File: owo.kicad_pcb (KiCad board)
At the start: 2 copper layers, 10.4 x 8.1 mm, 145 parts, among them J1 SJ-43515RS-SMT-TR, J2 SJ-43515RS-SMT-TR, J3 5051102291, J4 503398-1892, J5 2171840001, Q1 PMOS, Q2 NMOS, SW1 KMR221GLFS, SW2 KMR221GLFS, SW3 KMR221GLFS, SW4 KMR221GLFS, SW5 KMR221GLFS, SW6 KMR221GLFS, SW7 KMR221GLFS, U1 BQ24074RGT, U10 MCP23017_ML, U11 ESP32-C6-WROOM-1, U12 KMR241GLFS, U13 KMR241GLFS, U14 OPA1622, U2 TPS7A20xxxDQN, U3 LM27762, U4 TPS62840DLCR, U5 CD74HC4067M, U6 PCM5122PW, U7 OPA1622, U8 KMR241GLFS, U9 KMR241GLFS, X1 ASE-45.1584MHz, X2 ASE-24.576MHz, Y1 32.768kHz 9pF

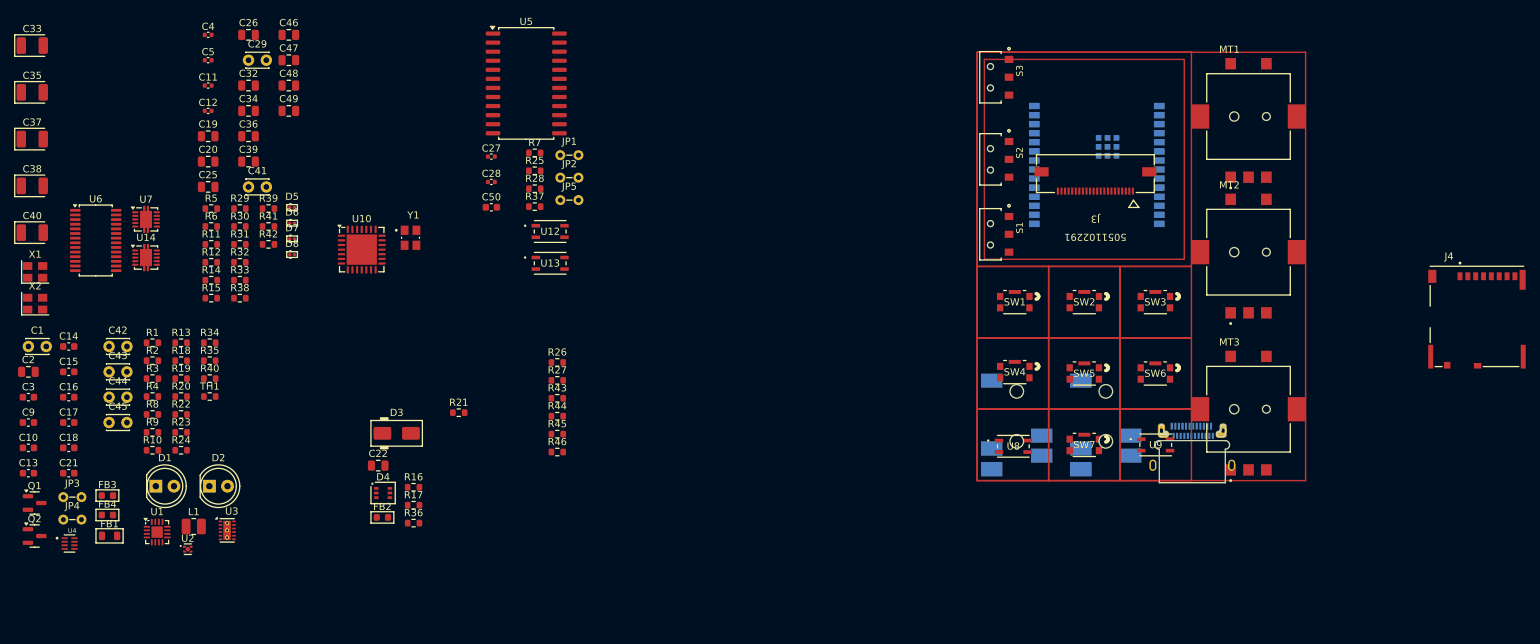
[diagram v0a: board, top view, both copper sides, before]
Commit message: ICs placed
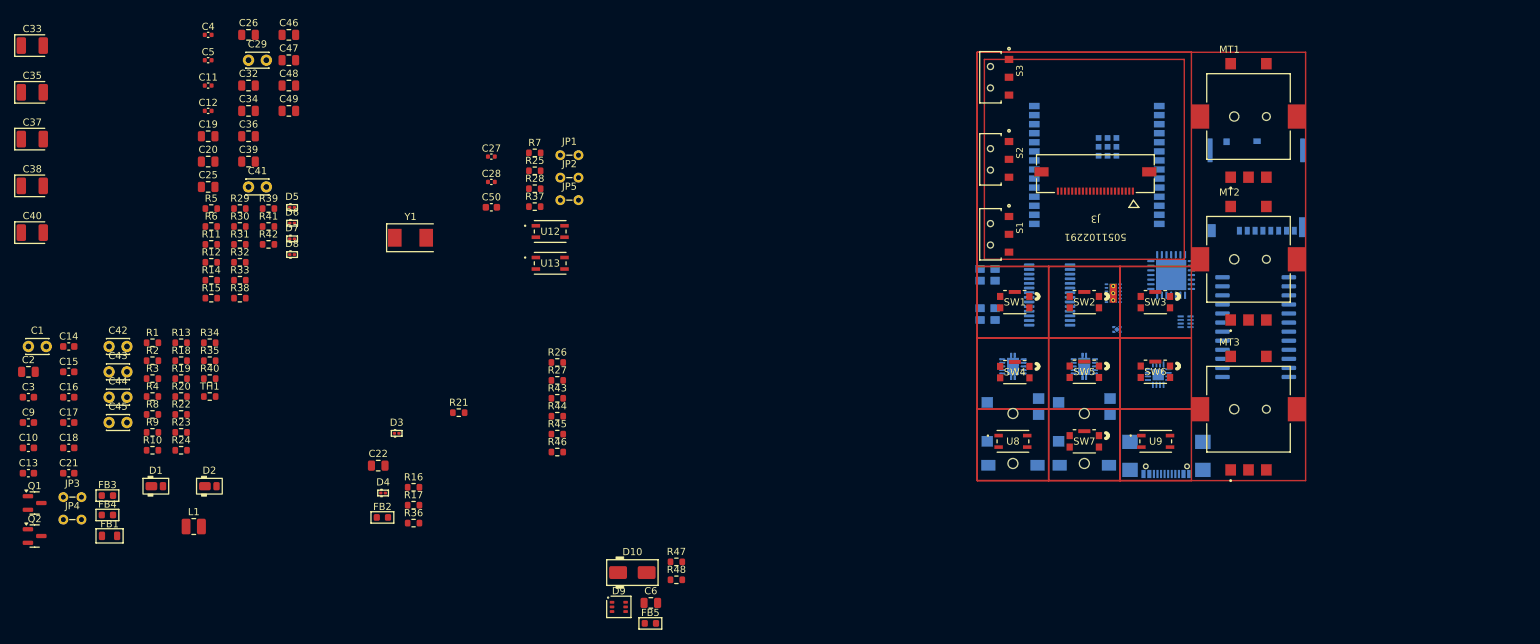
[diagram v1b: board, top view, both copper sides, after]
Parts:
- removed J5: 2171840001, uwu:MOLEX_2171840001
- added C6: 10uF/25V, Capacitor_SMD:C_0805_2012Metric, F.Cu at (100.3, 112.1)
- added D10: SS14, PCM_Diode_SMD_AKL:D_SMA, F.Cu at (97.7, 107.9)
- added D9: SMF05CT, PCM_Package_TO_SOT_SMD_AKL:SOT-363_SC-70-6, F.Cu at (95.8, 112.7)
- added FB5: 220@100MHz, PCM_Ferrite_SMD_AKL:Ferrite_0603_1608Metric, F.Cu at (100.2, 115.0)
- added J6: USB4110GFA, uwu:GCT_USB4110GFA, B.Cu at (172.5, 93.0)
- added R47: 1.1k, Resistor_SMD:R_0603_1608Metric, F.Cu at (103.9, 106.4)
- added R48: 1.1k, Resistor_SMD:R_0603_1608Metric, F.Cu at (103.9, 108.9)
- D1, D2: footprint LED_THT:LED_D5.0mm -> PCM_LED_SMD_AKL:LED_PLCC-2_2216
- D3: value SS14 -> SP1005-01WTG; footprint PCM_Diode_SMD_AKL:D_SMA -> PCM_Diode_SMD_AKL:D_0201_0603Metric
- D4: value SMF05CT -> SP1005-01WTG; footprint PCM_Package_TO_SOT_SMD_AKL:SOT-363_SC-70-6 -> PCM_Diode_SMD_AKL:D_0201_0603Metric
- J1, J2: value SJ-43515RS-SMT-TR -> SJ-43516-SMT-TR; footprint uwu:CUI_SJ-43515RS-SMT-TR -> uwu:CUI_SJ2-35894D-SMT-TR
- J4, U1, U10, U14, U2, U3, U4, U5, U6, U7, X1, X2: moved to B.Cu
- R14, R15: value 100 -> 10
- Y1: footprint uwu:XTAL_ASE-24.576MHZ-LC-T -> Crystal:Crystal_SMD_0603-2Pin_6.0x3.5mm
- moved U4 159.4 mm to (175.2, 72.8), turned to 180 degrees
- moved U1 142.0 mm to (171.4, 80.2), turned to 180 degrees
- moved U6 133.8 mm to (156.1, 69.0), turned to 180 degrees
- moved U2 133.7 mm to (165.6, 73.8), turned to 180 degrees
- moved X2 133.4 mm to (147.4, 71.7), turned to 180 degrees
- moved X1 133.4 mm to (147.4, 66.2), turned to 180 degrees
- moved U7 133.0 mm to (161.0, 79.0), turned to 180 degrees
- moved U3 128.5 mm to (165.1, 68.8), turned to 180 degrees
- moved U14 122.4 mm to (151.0, 79.0), turned to 180 degrees
- moved U10 113.4 mm to (173.2, 66.2), turned to 180 degrees
- moved U5 107.7 mm to (185.0, 73.5), turned to 180 degrees
- moved J4 35.6 mm to (185.1, 54.4)
- moved J2 13.7 mm to (161.0, 89.0)
- moved J1 10.5 mm to (151.0, 89.0)
- moved MT2 1.00 mm to (184.0, 64.0)
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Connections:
- D3 pad 2: USB_VBUS -> AGND
- D4 pad 1: USB_VBUS -> Net-(D4-K)
- D4 pad 2: GND -> AGND
- J1 pad 2: Net-(D8-K) -> Net-(D4-K)
- J1 pad 3: Net-(D7-K) -> Net-(D3-K)
- R14 pad 2: Net-(D8-K) -> Net-(D4-K)
- R15 pad 1: LINEOUT_L -> LINEOUT_R
- R15 pad 2: Net-(D7-K) -> Net-(D3-K)
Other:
- board outline removed

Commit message: all pcb elements positioned + minor schematics changes
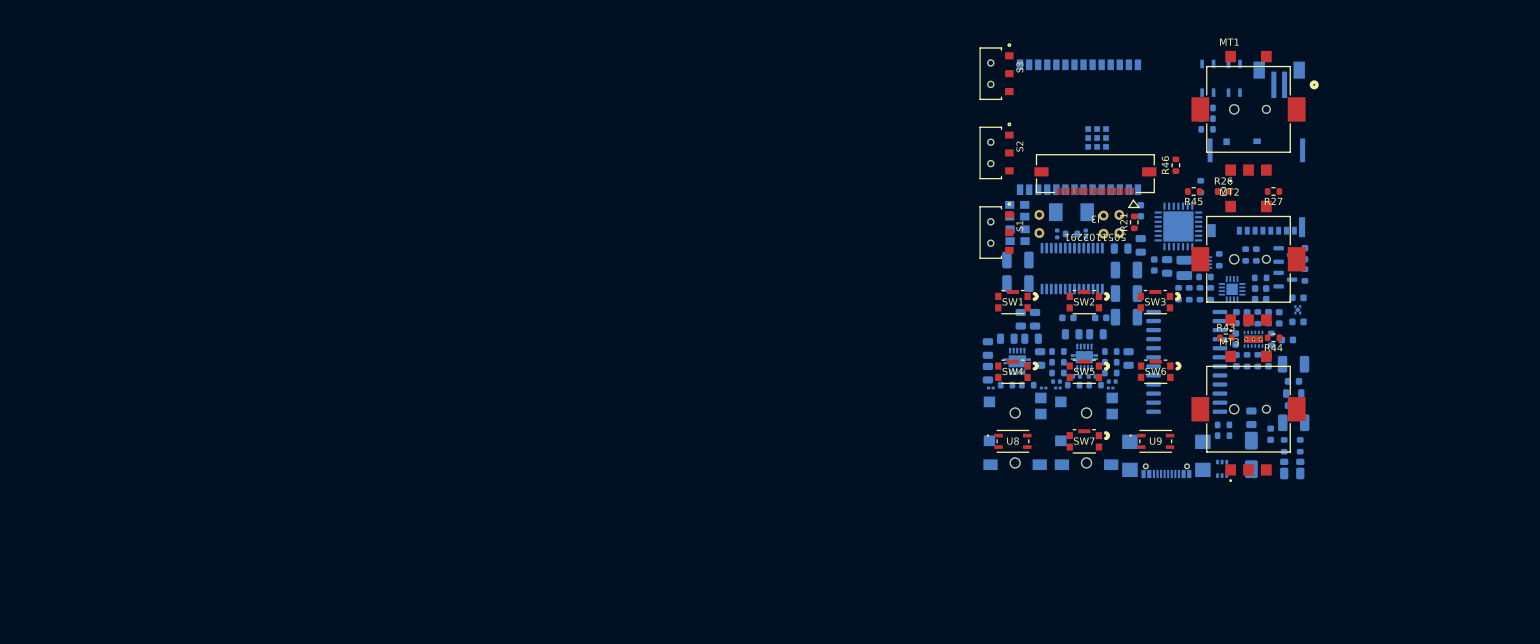
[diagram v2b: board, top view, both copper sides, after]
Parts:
- removed C22: 10uF/25V, Capacitor_SMD:C_0805_2012Metric
- removed D7, D8: SP1005-01WTG, PCM_Diode_SMD_AKL:D_0201_0603Metric
- removed FB2: 220@100MHz, PCM_Ferrite_SMD_AKL:Ferrite_0603_1608Metric
- removed JP3, JP4: Jumper_2_Bridged, PCM_Jumper_AKL:Jumper_P2.54mm_D0.7mm
- removed R16, R17: 1.1k, Resistor_SMD:R_0603_1608Metric
- removed R20: 10k, Resistor_SMD:R_0603_1608Metric
- removed R33, R38, R39, R41, R42: 0, Resistor_SMD:R_0603_1608Metric
- added J5: 3.7V, uwu:CONN_B2B-ZR-SM4-TF_JST, B.Cu at (189.0, 39.6)
- C1: value Capacitor_NP -> 1uF; footprint Capacitor_THT:C_Disc_D3.0mm_W2.0mm_P2.50mm -> Capacitor_SMD:C_0603_1608Metric; moved to B.Cu
- C10, C11, C12, C13, C14, C15, C16, C17, C18, C19, C2, C20, C21, C25, C26, C27, C28, C3, C32, C33, C34, C35, C36, C37, C38, C39, C4, C40, C46, C47, C48, C49, C5, C50, C6, C9, D1, D10, D2, D3, D4, D5, D6, D9, FB1, FB3, FB4, FB5, JP1, JP2, JP5, L1, Q1, Q2, R1, R10, R11, R12, R13, R14, R15, R18, R19, R2, R22, R23, R24, R25, R28, R29, R3, R30, R31, R32, R34, R35, R36, R37, R4, R40, R47, R48, R5, R6, R7, R8, R9, TH1, U12, U13, Y1: moved to B.Cu
- C29, C41: footprint Capacitor_THT:C_Disc_D3.0mm_W2.0mm_P2.50mm -> Capacitor_SMD:C_0603_1608Metric; moved to B.Cu
- C42, C44: value Capacitor_NP -> 10uF; footprint Capacitor_THT:C_Disc_D3.0mm_W2.0mm_P2.50mm -> Capacitor_Tantalum_SMD:CP_EIA-3528-21_Kemet-B; moved to B.Cu
- C43, C45: value Capacitor_NP -> 0.1uF; footprint Capacitor_THT:C_Disc_D3.0mm_W2.0mm_P2.50mm -> Capacitor_SMD:C_0603_1608Metric; moved to B.Cu
- moved Q2 179.6 mm to (189.2, 63.4)
- moved C10 178.7 mm to (190.9, 72.8), turned to 180 degrees
- moved Q1 178.0 mm to (189.2, 66.8)
- moved C1 176.4 mm to (189.4, 75.3)
- moved C13 174.4 mm to (186.8, 78.2), turned to 90 degrees
- moved C16 174.3 mm to (191.9, 63.2), turned to 90 degrees
- moved C15 172.5 mm to (190.9, 69.4)
- moved C9 169.8 mm to (182.3, 72.2), turned to -90 degrees
- moved C21 169.5 mm to (186.8, 72.2), turned to -90 degrees
- moved C18 168.3 mm to (185.7, 69.6)
- moved C17 168.0 mm to (185.7, 68.1), turned to 180 degrees
- moved FB1 167.1 mm to (190.3, 82.8)
- moved FB4 166.5 mm to (188.3, 72.2), turned to 90 degrees
- moved C42 166.3 mm to (190.3, 86.9), turned to 180 degrees
- moved C45 166.0 mm to (190.3, 81.1)
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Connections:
- C27 pad 1: AGND -> GND
- C28 pad 1: AGND -> GND
- R18 pad 2: Net-(JP3-A) -> VSYS
- R19 pad 2: Net-(JP4-A) -> VSYS
- SW1 pad 5: (no net) -> GND
- SW2 pad 5: (no net) -> GND
- SW3 pad 5: (no net) -> GND
- SW4 pad 5: (no net) -> GND
- SW5 pad 5: (no net) -> GND
- SW6 pad 5: (no net) -> GND
- SW7 pad 5: (no net) -> GND
- U14 pad 10: Net-(R42-+) -> LINEOUT_R
- U14 pad 6: Net-(R41-+) -> LINEOUT_L
- U6 pad 16: Net-(R39--) -> GND
- U6 pad 20: Net-(R33-+) -> Net-(U6-SCK)
- U6 pad 24: Net-(R38--) -> GND
- X1 pad 3: Net-(R33--) -> Net-(U6-SCK)
- X2 pad 3: Net-(R33-+) -> Net-(U6-SCK)
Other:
- board text added: "1M"

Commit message: tracing ground and some power planes
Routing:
- added copper zone on In2.Cu, net AGND
- added copper zone on In2.Cu, net GND
- added copper zone on In1.Cu, net V3.3_ANA
- added copper zone on In1.Cu, net V5N_ANA
- added copper zone on In1.Cu, net V5P_ANA
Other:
- copper layers 2 -> 4
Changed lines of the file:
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@@
 	(paper "A4")
 	(layers
-		(0 "F.Cu" signal)
+		(0 "F.Cu" jumper)
+		(1 "In1.Cu" signal)
+		(2 "In2.Cu" signal)
 		(31 "B.Cu" signal)
 		(32 "B.Adhes" user "B.Adhesive")
@@
 	)
 	(setup
+		(stackup
+			(layer "F.SilkS"
+				(type "Top Silk Screen")
+			)
+			(layer "F.Paste"
+				(type "Top Solder Paste")
+			)
+			(layer "F.Mask"
+				(type "Top Solder Mask")
+				(thickness 0.01)
+			)
+			(layer "F.Cu"
+				(type "copper")
+				(thickness 0.035)
+			)
+			(layer "dielectric 1"
+				(type "prepreg")
+				(thickness 0.1)
+				(material "FR4")
+				(epsilon_r 4.5)
+				(loss_tangent 0.02)
+			)
+			(layer "In1.Cu"
+				(type "copper")
+				(thickness 0.035)
+			)
+			(layer "dielectric 2"
+				(type "core")
+				(thickness 1.24)
+				(material "FR4")
+				(epsilon_r 4.5)
+				(loss_tangent 0.02)
+			)
+			(layer "In2.Cu"
+				(type "copper")
+				(thickness 0.035)
+			)
+			(layer "dielectric 3"
+				(type "prepreg")
+				(thickness 0.1)
+				(material "FR4")
+				(epsilon_r 4.5)
+				(loss_tangent 0.02)
+			)
+			(layer "B.Cu"
+				(type "copper")
+				(thickness 0.035)
+			)
+			(layer "B.Mask"
+				(type "Bottom Solder Mask")
+				(thickness 0.01)
+			)
+			(layer "B.Paste"
+				(type "Bottom Solder Paste")
+			)
+			(layer "B.SilkS"
+				(type "Bottom Silk Screen")
+			)
+			(copper_finish "None")
+			(dielectric_constraints no)
+		)
 		(pad_to_mask_clearance 0)
 		(allow_soldermask_bridges_in_footprints no)
@@
 		)
 	)
+	(zone
+		(net 25)
+		(net_name "V5N_ANA")
+		(layer "In1.Cu")
+		(hatch edge 0.5)
+		(priority 3)
+		(connect_pads
+			(clearance 0.5)
+		)
+		(min_thickness 0.25)
+		(filled_areas_thickness no)
+		(fill
+			(thermal_gap 0.5)
+			(thermal_bridge_width 0.5)
+		)
+		(polygon
+			(pts
+				(xy 189.1 70.7) (xy 146.5 70.7) (xy 146.5 75) (xy 182.88449 74.9) (xy 182.9 73.7) (xy 186 73.7)
+				(xy 189.1 73.7) (xy 189.1 73.7)
+			)
+		)
+	)
+	(zone
+		(net 24)
+		(net_name "V5P_ANA")
+		(layer "In1.Cu")
+		(hatch edge 0.5)
+		(priority 2)
+		(connect_pads
+			(clearance 0.5)
+		)
+		(min_thickness 0.25)
+		(filled_areas_thickness no)
+		(fill
+			(thermal_gap 0.5)
+			(thermal_bridge_width 0.5)
+		)
+		(polygon
+			(pts
+				(xy 189.1 76.7) (xy 182.9 76.7) (xy 182.892465 75.5) (xy 146.5 75.5) (xy 146.5 79.7) (xy 189.1 79.7)
+			)
+		)
+	)
+	(zone
+		(net 18)
+		(net_name "V3.3_ANA")
+		(layer "In1.Cu")
+		(hatch edge 0.5)
+		(priority 4)
+		(connect_pads
+			(clearance 0.5)
+		)
+		(min_thickness 0.25)
+		(filled_areas_thickness no)
+		(fill
+			(thermal_gap 0.5)
+			(thermal_bridge_width 0.5)
+		)
+		(polygon
+			(pts
+				(xy 146.5 62.6) (xy 146.5 70.3) (xy 146.5 70.3) (xy 189.5 70.3) (xy 189.5 83.8) (xy 189.6 83.9)
+				(xy 192.8 83.9) (xy 192.8 62.6)
+			)
+		)
+	)
+	(zone
+		(net 7)
+		(net_name "AGND")
+		(layer "In2.Cu")
+		(hatch edge 0.5)
+		(connect_pads
+			(clearance 0.5)
+		)
+		(min_thickness 0.25)
+		(filled_areas_thickness no)
+		(fill
+			(thermal_gap 0.5)
+			(thermal_bridge_width 0.5)
+		)
+		(polygon
+			(pts
+				(xy 166 94.9) (xy 166.1 64.9) (xy 146.5 64.9) (xy 146.5 94.8) (xy 146.5 94.9)
+			)
+		)
+	)
+	(zone
+		(net 4)
+		(net_name "GND")
+		(layer "In2.Cu")
+		(hatch edge 0.5)
+		(priority 1)
+		(connect_pads
+			(clearance 0.5)
+		)
+		(min_thickness 0.25)
+		(filled_areas_thickness no)
+		(fill
+			(thermal_gap 0.5)
+			(thermal_bridge_width 0.5)
+		)
+		(polygon
+			(pts
+				(xy 149 64.1) (xy 166.9 64.1) (xy 166.9 94.9) (xy 192.8 94.9) (xy 192.8 34.4) (xy 192.8 34.4) (xy 149 34.4)
+			)
+		)
+	)

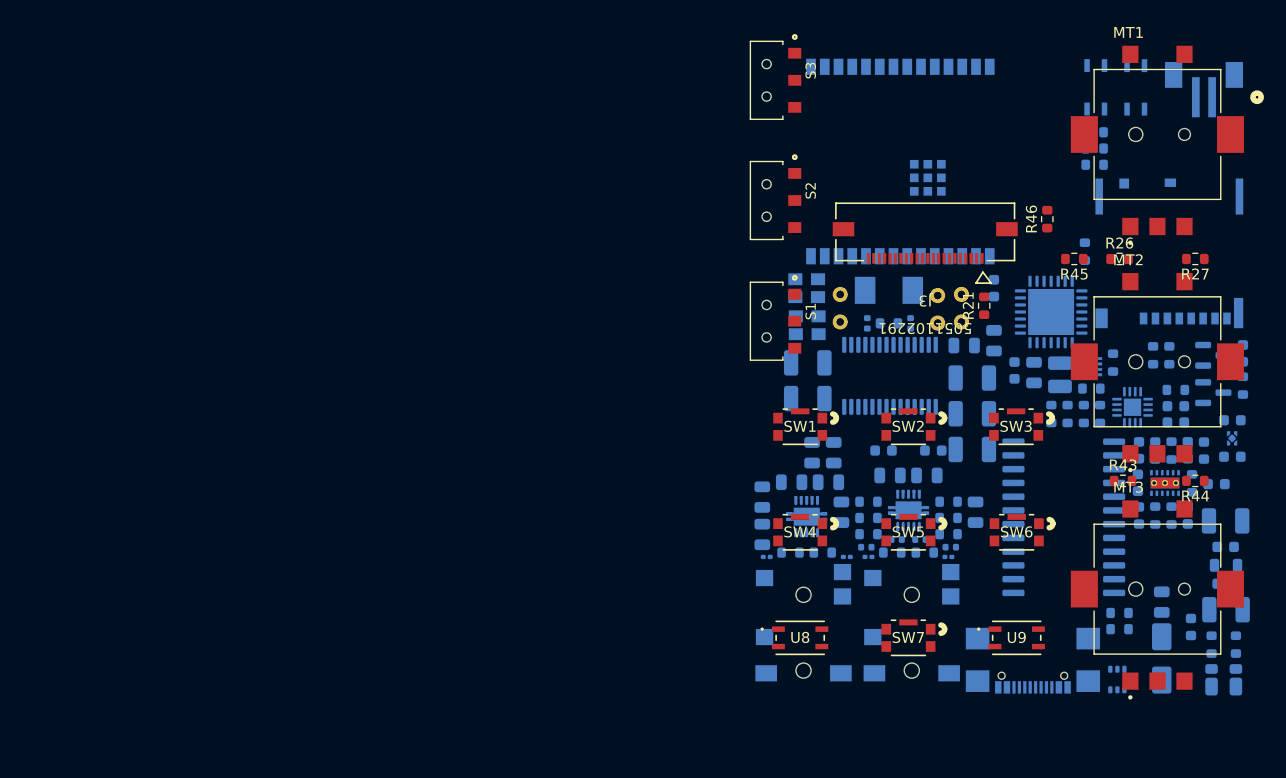
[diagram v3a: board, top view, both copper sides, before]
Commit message: changing ic placement
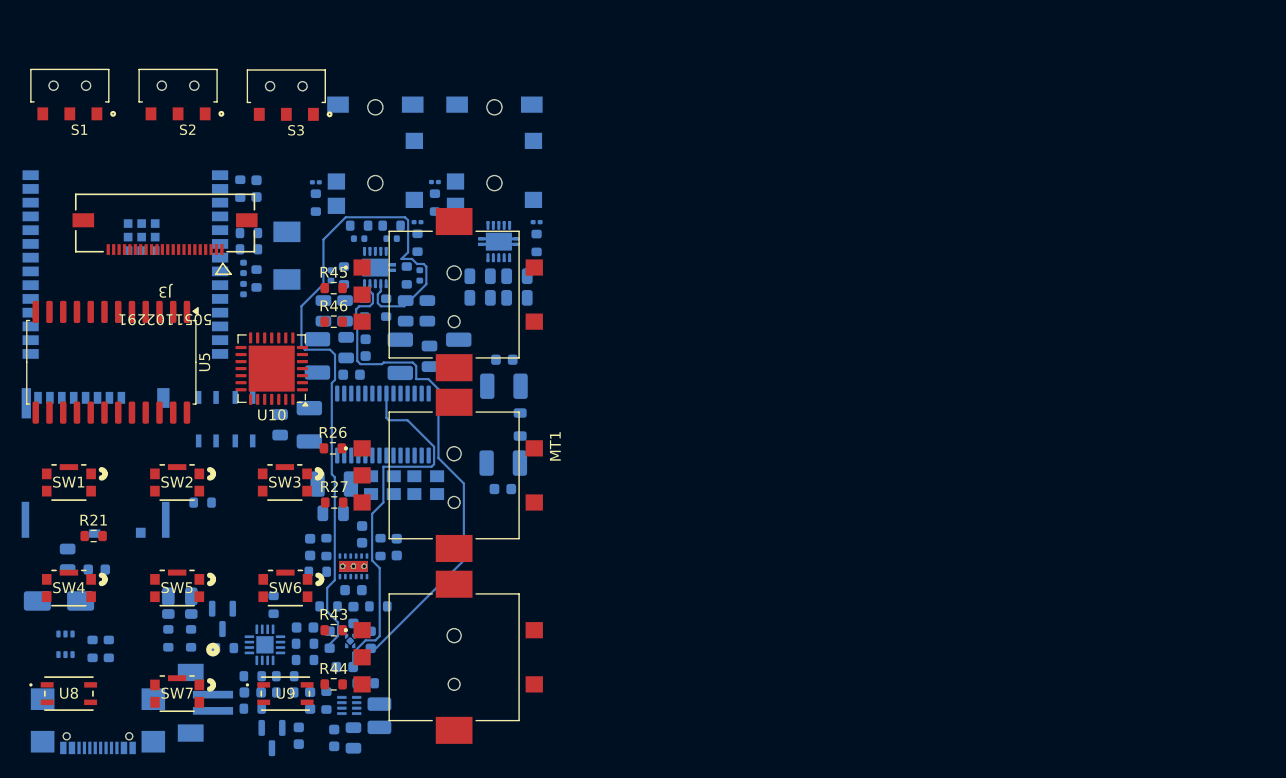
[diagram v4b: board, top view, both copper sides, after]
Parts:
- removed JP1, JP2, JP5: Jumper_2_Bridged, PCM_Jumper_AKL:Jumper_P2.54mm_D0.7mm
- U10, U5: moved to F.Cu
- moved J5 107.5 mm to (96.8, 94.7), turned to -90 degrees
- moved D10 102.0 mm to (82.5, 86.1), turned to 0 degrees
- moved FB5 101.2 mm to (86.0, 83.2), turned to 0 degrees
- moved C6 101.1 mm to (83.3, 82.2)
- moved J4 100.9 mm to (85.9, 73.0), turned to 180 degrees
- moved D1 98.9 mm to (92.6, 86.3), turned to -90 degrees
- moved R18 98.6 mm to (92.6, 89.5), turned to -90 degrees
- moved D9 97.2 mm to (83.1, 90.1), turned to -90 degrees
- moved R35 96.2 mm to (100.4, 96.0), turned to 180 degrees
- moved R47 94.9 mm to (85.6, 90.5), turned to 90 degrees
- moved D2 94.5 mm to (94.8, 86.3), turned to -90 degrees
- moved R19 94.3 mm to (94.7, 89.5), turned to -90 degrees
- moved C16 94.1 mm to (104.7, 98.5)
- moved Q1 93.9 mm to (97.6, 87.7), turned to -90 degrees
- moved Q2 93.9 mm to (102.2, 98.8), turned to -90 degrees
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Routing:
- net V5P_ANA: track 0.00 -> 66.7 mm
- net V5N_ANA: track 0.00 -> 46.7 mm
- net V3.3_ANA: track 0.00 -> 34.9 mm
- removed copper zone on In2.Cu, net GND
- removed copper zone on In1.Cu, net V3.3_ANA
- removed copper zone on In1.Cu, net V5N_ANA
- removed copper zone on In1.Cu, net V5P_ANA
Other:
- copper layers 4 -> 6
- board text removed: "1M"

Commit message: routing
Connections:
- net Net-(L1-+) renamed BUCK
- C27 pad 2: Net-(JP1-A) -> Net-(R25-+)
- C28 pad 2: Net-(JP2-B) -> Net-(R25--)
- C50 pad 1: Net-(JP5-B) -> V3.3_SYS
- FB3 pad 2: V5P_ANA -> V5N_ANA
- J1 pad 10: JACK_AUDIO_SW -> JACK_LINE_SW
- J1 pad 11: JACK_AUDIO_SW -> JACK_LINE_SW
- MT2 pad B: ENC2_B -> V5N_ANA
- R25 pad 1: Net-(JP1-A) -> Net-(R25-+)
- R25 pad 2: Net-(JP2-B) -> Net-(R25--)
- R37 pad 2: Net-(JP5-B) -> V3.3_SYS
- R44 pad 2: ENC2_B -> V5N_ANA
- U10 pad 18: AUDIO_EN -> JACK_EN
- U10 pad 19: BAT_LEVEL -> LINEOUT_EN
- U10 pad 27: ENC2_B -> V5N_ANA
- U11 pad 3: Net-(JP5-B) -> V3.3_SYS
- U11 pad 8: Net-(JP1-B) -> Net-(R25-+)
- U11 pad 9: Net-(JP2-A) -> Net-(R25--)
- U12 pad 1: Net-(JP5-B) -> V3.3_SYS
- U12 pad 4: Net-(JP5-B) -> V3.3_SYS
- U13 pad 1: Net-(JP1-B) -> Net-(R25-+)
- U13 pad 4: Net-(JP1-B) -> Net-(R25-+)
- U14 pad 8: V3.3_ANA -> LINEOUT_EN
- U5 pad 17: unconnected-(U5-I14-Pad17) -> BAT_LEVEL
- U7 pad 8: V3.3_SYS -> JACK_EN
- Y1 pad 1: Net-(JP1-A) -> Net-(R25-+)
- Y1 pad 2: Net-(JP2-B) -> Net-(R25--)
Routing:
- net GND: track 0.00 -> 237.5 mm, vias 0 -> 83
- net V3.3_SYS: track 0.00 -> 104.5 mm, vias 0 -> 25
- net AGND: track 0.00 -> 92.7 mm, vias 0 -> 21
- net JACK_LINE_SW: track 0.00 -> 60.2 mm, vias 0 -> 3
- net USB_DN: track 0.00 -> 54.9 mm, vias 0 -> 4
- net BAT_LEVEL: track 0.00 -> 51.0 mm, vias 0 -> 3
- net ENC3_SW1: track 0.00 -> 50.3 mm, vias 0 -> 2
- net SWITCH_1: track 0.00 -> 49.0 mm, vias 0 -> 3
- net USB_DP: track 0.00 -> 48.5 mm, vias 0 -> 3
- net I2S_DIN: track 0.00 -> 46.8 mm, vias 0 -> 3
- net ESP_SDA: track 0.00 -> 46.7 mm, vias 0 -> 4
- net ENC2_SW1: track 0.00 -> 46.7 mm, vias 0 -> 2
- net BTN_8: track 0.00 -> 43.0 mm, vias 0 -> 2
- net I2S_BCK: track 0.00 -> 42.0 mm, vias 0 -> 2
- net LINEOUT_EN: track 0.00 -> 40.8 mm, vias 0 -> 3
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- added copper zone on In4.Cu, net AGND
- added copper zone on In1.Cu, net GND
- added copper zone on In4.Cu, net GND
- added copper zone on F.Cu, net V3.3_ANA
- added copper zone on In3.Cu, net V3.3_ANA
- added copper zone on In2.Cu, net V3.3_SYS
- added copper zone on In3.Cu, net V5N_ANA
- added copper zone on In3.Cu, net V5P_ANA
- removed copper zone on In2.Cu, net AGND
